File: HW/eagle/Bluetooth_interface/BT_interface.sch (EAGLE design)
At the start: 46 parts, among them IC3 FT232RL, IC5 UA78M05DCY

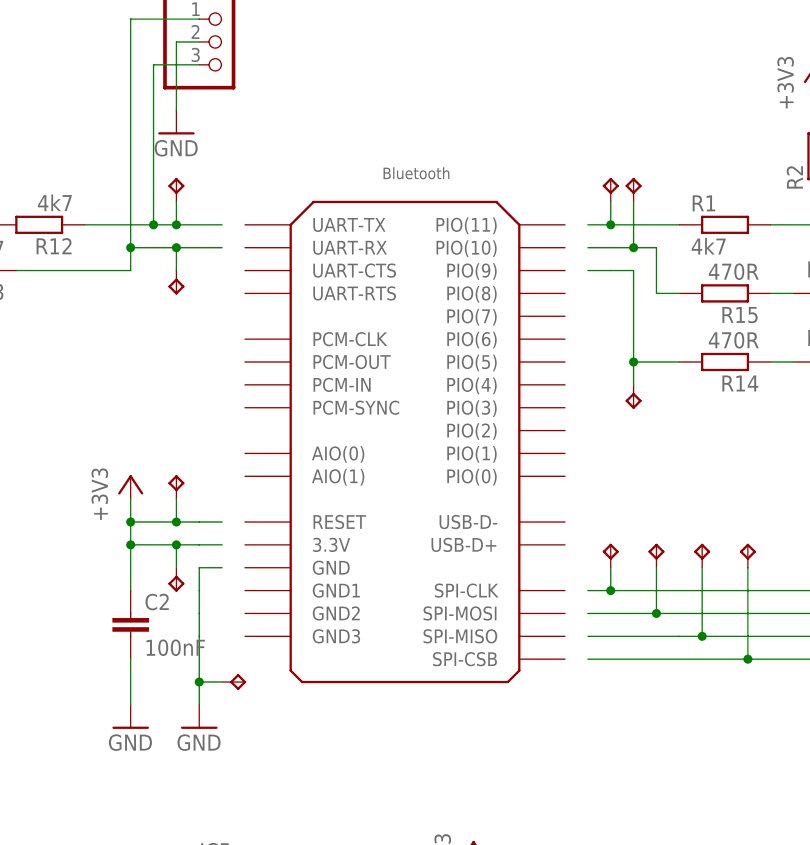
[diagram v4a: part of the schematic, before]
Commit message: bluetooth module footprint removed and replaced with dummy drawing
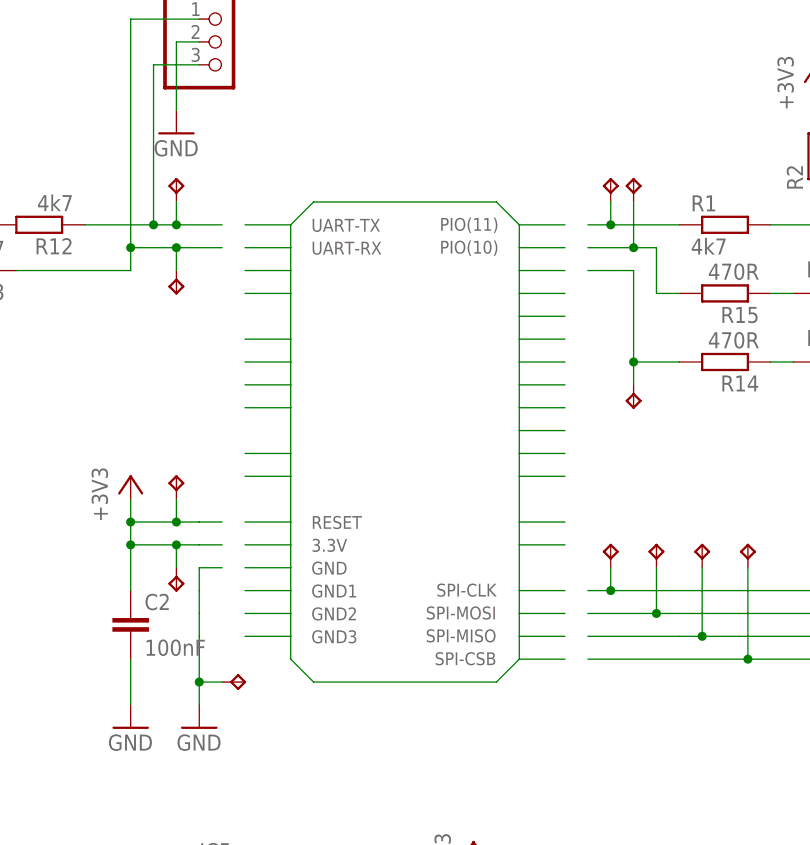
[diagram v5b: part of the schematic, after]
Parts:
- removed U$1: BLUETOOTH, daGloane:BLUETOOTH
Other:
- note added: "3.3V"
- note added: "GND"
- note added: "GND1"
- note added: "GND2"
- note added: "GND3"
- note added: "PIO(10)"
- note added: "PIO(11)"
- note added: "RESET"
- note added: "SPI-CLK"
- note added: "SPI-CSB"
- note added: "SPI-MISO"
- note added: "SPI-MOSI"
- note added: "UART-RX"
- note added: "UART-TX"
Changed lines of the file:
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@@
 <part name="+3V1" library="supply1" deviceset="+3V3" device=""/>
 <part name="GND1" library="supply1" deviceset="GND" device=""/>
-<part name="U$1" library="daGloane" deviceset="BLUETOOTH" device=""/>
 <part name="C1" library="rcl" deviceset="C-EU" device="C0805" value="10µ"/>
 <part name="+3V2" library="supply1" deviceset="+3V3" device=""/>
@@
 <text x="96.56" y="71.16" size="1.778" layer="94">FT232RL</text>
 <text x="12.74" y="53.38" size="1.778" layer="94" rot="R90">Mini-USB-B</text>
+<text x="225.806" y="108.458" size="1.4224" layer="95">UART-TX</text>
+<text x="225.806" y="105.918" size="1.4224" layer="95">UART-RX</text>
+<text x="225.806" y="75.438" size="1.4224" layer="95">RESET</text>
+<text x="225.806" y="72.898" size="1.4224" layer="95">3.3V</text>
+<text x="225.806" y="70.358" size="1.4224" layer="95">GND</text>
+<text x="225.806" y="67.818" size="1.4224" layer="95">GND1</text>
+<text x="225.806" y="65.278" size="1.4224" layer="95">GND2</text>
+<text x="225.806" y="62.738" size="1.4224" layer="95">GND3</text>
+<text x="246.38" y="61.722" size="1.4224" layer="95" rot="R180">SPI-CSB</text>
+<text x="246.38" y="64.262" size="1.4224" layer="95" rot="R180">SPI-MISO</text>
+<text x="246.38" y="66.802" size="1.4224" layer="95" rot="R180">SPI-MOSI</text>
+<text x="246.38" y="69.342" size="1.4224" layer="95" rot="R180">SPI-CLK</text>
+<text x="246.634" y="109.982" size="1.4224" layer="95" rot="R180">PIO(11)</text>
+<text x="246.634" y="107.442" size="1.4224" layer="95" rot="R180">PIO(10)</text>
 </plain>
 <instances>
@@
 <instance part="+3V1" gate="G$1" x="243.84" y="40.64"/>
 <instance part="GND1" gate="1" x="203.2" y="17.78"/>
-<instance part="U$1" gate="G$1" x="243.84" y="93.98"/>
 <instance part="C1" gate="G$1" x="203.2" y="27.94"/>
 <instance part="+3V2" gate="G$1" x="205.74" y="81.28"/>
@@
 </segment>
 </net>
+<net name="N$17" class="0">
+<segment>
+<wire x1="223.52" y1="109.22" x2="226.06" y2="111.76" width="0.1524" layer="91"/>
+<wire x1="226.06" y1="111.76" x2="246.38" y2="111.76" width="0.1524" layer="91"/>
+<wire x1="246.38" y1="111.76" x2="248.92" y2="109.22" width="0.1524" layer="91"/>
+<wire x1="248.92" y1="109.22" x2="248.92" y2="106.68" width="0.1524" layer="91"/>
+<wire x1="248.92" y1="106.68" x2="248.92" y2="104.14" width="0.1524" layer="91"/>
+<wire x1="248.92" y1="104.14" x2="248.92" y2="101.6" width="0.1524" layer="91"/>
+<wire x1="248.92" y1="101.6" x2="248.92" y2="99.06" width="0.1524" layer="91"/>
+<wire x1="248.92" y1="99.06" x2="248.92" y2="96.52" width="0.1524" layer="91"/>
+<wire x1="248.92" y1="96.52" x2="248.92" y2="93.98" width="0.1524" layer="91"/>
+<wire x1="248.92" y1="93.98" x2="248.92" y2="91.44" width="0.1524" layer="91"/>
+<wire x1="248.92" y1="91.44" x2="248.92" y2="88.9" width="0.1524" layer="91"/>
+<wire x1="248.92" y1="88.9" x2="248.92" y2="86.36" width="0.1524" layer="91"/>
+<wire x1="248.92" y1="86.36" x2="248.92" y2="83.82" width="0.1524" layer="91"/>
+<wire x1="248.92" y1="83.82" x2="248.92" y2="81.28" width="0.1524" layer="91"/>
+<wire x1="248.92" y1="81.28" x2="248.92" y2="76.2" width="0.1524" layer="91"/>
+<wire x1="248.92" y1="76.2" x2="248.92" y2="73.66" width="0.1524" layer="91"/>
+<wire x1="248.92" y1="73.66" x2="248.92" y2="68.58" width="0.1524" layer="91"/>
+<wire x1="248.92" y1="68.58" x2="248.92" y2="66.04" width="0.1524" layer="91"/>
+<wire x1="248.92" y1="66.04" x2="248.92" y2="63.5" width="0.1524" layer="91"/>
+<wire x1="248.92" y1="63.5" x2="248.92" y2="60.96" width="0.1524" layer="91"/>
+<wire x1="248.92" y1="60.96" x2="246.38" y2="58.42" width="0.1524" layer="91"/>
+<wire x1="246.38" y1="58.42" x2="226.06" y2="58.42" width="0.1524" layer="91"/>
+<wire x1="226.06" y1="58.42" x2="223.52" y2="60.96" width="0.1524" layer="91"/>
+<wire x1="223.52" y1="60.96" x2="223.52" y2="63.5" width="0.1524" layer="91"/>
+<wire x1="223.52" y1="63.5" x2="223.52" y2="66.04" width="0.1524" layer="91"/>
+<wire x1="223.52" y1="66.04" x2="223.52" y2="68.58" width="0.1524" layer="91"/>
+<wire x1="223.52" y1="68.58" x2="223.52" y2="71.12" width="0.1524" layer="91"/>
+<wire x1="223.52" y1="71.12" x2="223.52" y2="73.66" width="0.1524" layer="91"/>
+<wire x1="223.52" y1="73.66" x2="223.52" y2="76.2" width="0.1524" layer="91"/>
+<wire x1="223.52" y1="76.2" x2="223.52" y2="81.28" width="0.1524" layer="91"/>
+<wire x1="223.52" y1="81.28" x2="223.52" y2="83.82" width="0.1524" layer="91"/>
+<wire x1="223.52" y1="83.82" x2="223.52" y2="88.9" width="0.1524" layer="91"/>
+<wire x1="223.52" y1="88.9" x2="223.52" y2="91.44" width="0.1524" layer="91"/>
+<wire x1="223.52" y1="91.44" x2="223.52" y2="93.98" width="0.1524" layer="91"/>
+<wire x1="223.52" y1="93.98" x2="223.52" y2="96.52" width="0.1524" layer="91"/>
+<wire x1="223.52" y1="96.52" x2="223.52" y2="101.6" width="0.1524" layer="91"/>
+<wire x1="223.52" y1="101.6" x2="223.52" y2="104.14" width="0.1524" layer="91"/>
+<wire x1="223.52" y1="104.14" x2="223.52" y2="106.68" width="0.1524" layer="91"/>
+<wire x1="223.52" y1="106.68" x2="223.52" y2="109.22" width="0.1524" layer="91"/>
+<wire x1="223.52" y1="109.22" x2="218.44" y2="109.22" width="0.1524" layer="91"/>
+<wire x1="218.44" y1="106.68" x2="223.52" y2="106.68" width="0.1524" layer="91"/>
+<wire x1="218.44" y1="104.14" x2="223.52" y2="104.14" width="0.1524" layer="91"/>
+<wire x1="218.44" y1="101.6" x2="223.52" y2="101.6" width="0.1524" layer="91"/>
+<wire x1="218.44" y1="96.52" x2="223.52" y2="96.52" width="0.1524" layer="91"/>
+<wire x1="218.44" y1="93.98" x2="223.52" y2="93.98" width="0.1524" layer="91"/>
+<wire x1="218.44" y1="91.44" x2="223.52" y2="91.44" width="0.1524" layer="91"/>
+<wire x1="218.44" y1="88.9" x2="223.52" y2="88.9" width="0.1524" layer="91"/>
+<wire x1="218.44" y1="83.82" x2="223.52" y2="83.82" width="0.1524" layer="91"/>
+<wire x1="218.44" y1="81.28" x2="223.52" y2="81.28" width="0.1524" layer="91"/>
+<wire x1="218.44" y1="76.2" x2="223.52" y2="76.2" width="0.1524" layer="91"/>
+<wire x1="218.44" y1="73.66" x2="223.52" y2="73.66" width="0.1524" layer="91"/>
+<wire x1="218.44" y1="71.12" x2="223.52" y2="71.12" width="0.1524" layer="91"/>
+<wire x1="218.44" y1="68.58" x2="223.52" y2="68.58" width="0.1524" layer="91"/>
+<wire x1="218.44" y1="66.04" x2="223.52" y2="66.04" width="0.1524" layer="91"/>
+<wire x1="218.44" y1="63.5" x2="223.52" y2="63.5" width="0.1524" layer="91"/>
+<wire x1="248.92" y1="60.96" x2="254" y2="60.96" width="0.1524" layer="91"/>
+<wire x1="248.92" y1="63.5" x2="254" y2="63.5" width="0.1524" layer="91"/>
+<wire x1="248.92" y1="66.04" x2="254" y2="66.04" width="0.1524" layer="91"/>
+<wire x1="248.92" y1="68.58" x2="254" y2="68.58" width="0.1524" layer="91"/>
+<wire x1="248.92" y1="73.66" x2="254" y2="73.66" width="0.1524" layer="91"/>
+<wire x1="248.92" y1="76.2" x2="254" y2="76.2" width="0.1524" layer="91"/>
+<wire x1="248.92" y1="81.28" x2="254" y2="81.28" width="0.1524" layer="91"/>
+<wire x1="248.92" y1="83.82" x2="254" y2="83.82" width="0.1524" layer="91"/>
+<wire x1="248.92" y1="86.36" x2="254" y2="86.36" width="0.1524" layer="91"/>
+<wire x1="248.92" y1="88.9" x2="254" y2="88.9" width="0.1524" layer="91"/>
+<wire x1="248.92" y1="91.44" x2="254" y2="91.44" width="0.1524" layer="91"/>
+<wire x1="248.92" y1="93.98" x2="254" y2="93.98" width="0.1524" layer="91"/>
+<wire x1="248.92" y1="96.52" x2="254" y2="96.52" width="0.1524" layer="91"/>
+<wire x1="248.92" y1="99.06" x2="254" y2="99.06" width="0.1524" layer="91"/>
+<wire x1="248.92" y1="101.6" x2="254" y2="101.6" width="0.1524" layer="91"/>
+<wire x1="248.92" y1="104.14" x2="254" y2="104.14" width="0.1524" layer="91"/>
+<wire x1="248.92" y1="106.68" x2="254" y2="106.68" width="0.1524" layer="91"/>
+<wire x1="248.92" y1="109.22" x2="254" y2="109.22" width="0.1524" layer="91"/>
+</segment>
+</net>

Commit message: .
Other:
- note added: "Bluetooth Module"
- moved on the sheet: C1, C14, C16, C17, C18, C2, C25, C29, IC3, IC5, LED1, LED2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
